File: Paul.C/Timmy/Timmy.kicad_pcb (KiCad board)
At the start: 2 copper layers, 34 parts, among them J1 I/O, J2 Power, J3 LED, SW1 SW_DIP_x02, U1 NJM4559

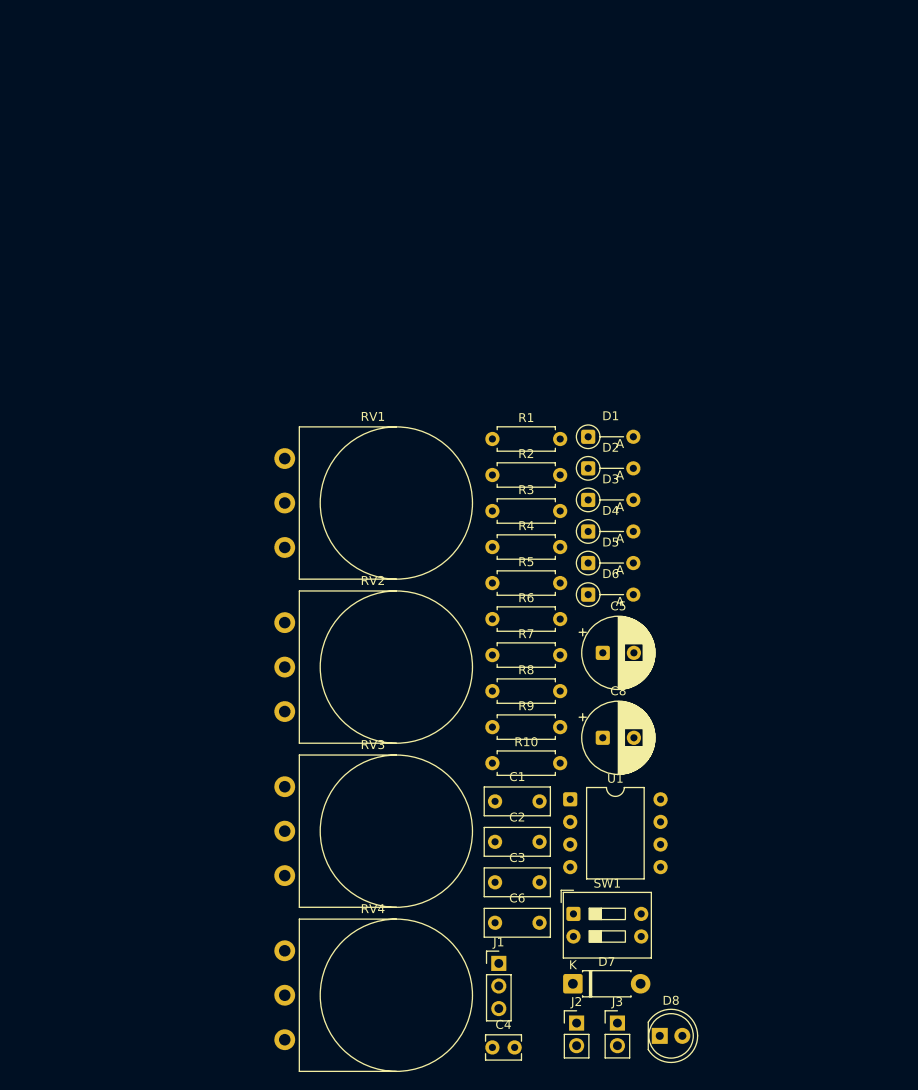
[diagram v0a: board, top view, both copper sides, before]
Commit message: feat: フットプリントを紐づけ
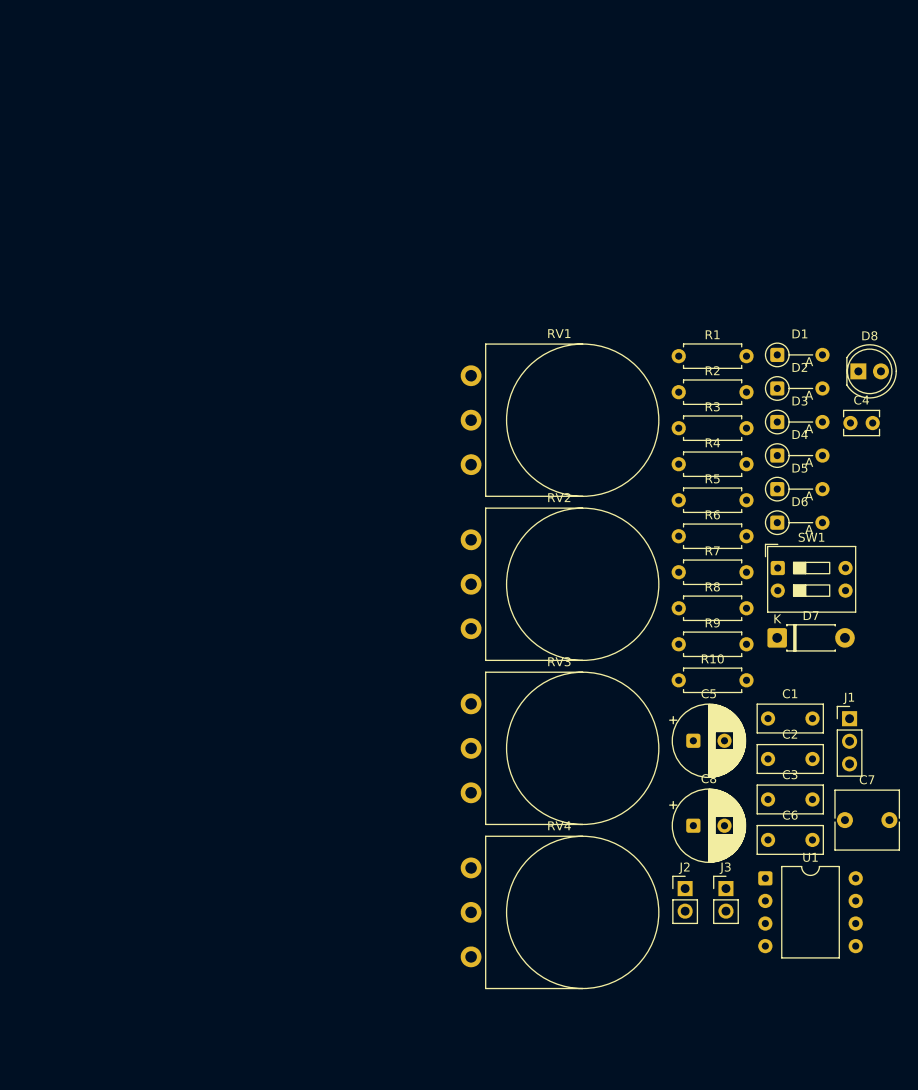
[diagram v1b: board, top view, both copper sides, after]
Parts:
- added C7: 1u, Capacitor_THT:C_Rect_L7.0mm_W6.5mm_P5.00mm, F.Cu at (170.5, 116.8)
- moved C4 80.9 mm to (171.1, 72.1)
- moved D8 78.0 mm to (172.0, 66.3)
- moved J1 48.1 mm to (171.0, 105.4)
- moved D7 45.2 mm to (162.9, 96.3)
- moved SW1 45.2 mm to (162.9, 88.4)
- moved C1 32.1 mm to (161.8, 105.3)
- moved C2 32.1 mm to (161.8, 109.9)
- moved C3 32.1 mm to (161.8, 114.5)
- moved C6 32.1 mm to (161.8, 119.0)
- moved U1 23.7 mm to (161.5, 123.3)
- moved D1 23.2 mm to (162.9, 64.5)
- moved D2 23.1 mm to (162.9, 68.2)
- moved D3 23.0 mm to (162.9, 72.0)
- moved RV1 22.9 mm to (128.4, 76.8)
- moved RV2 22.9 mm to (128.4, 95.2)
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
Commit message: feat: ReLayout Paul.C/Timmy
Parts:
- removed J1: I/O, Connector_PinHeader_2.54mm:PinHeader_1x03_P2.54mm_Vertical
- added J2: Power, Connector_PinHeader_2.54mm:PinHeader_1x02_P2.54mm_Vertical, F.Cu at (128.3, 55.8)
- added J5: INPUT, Connector_PinHeader_2.54mm:PinHeader_1x01_P2.54mm_Vertical, F.Cu at (97.8, 77.3)
- C4: value 100p -> 101
- D8, RV1, RV2, RV3: moved to B.Cu
- RV4: value A50k -> A10k; moved to B.Cu
- moved J3 93.3 mm to (99.8, 47.5), turned to 180 degrees
- moved J4 89.6 mm to (111.2, 47.5), turned to 180 degrees
- moved U1 83.4 mm to (100.4, 66.6)
- moved RV4 82.3 mm to (117.0, 50.7), turned to 90 degrees
- moved D5 80.8 mm to (82.6, 69.7), turned to 90 degrees
- moved D6 79.9 mm to (85.2, 64.7), turned to -90 degrees
- moved C2 78.3 mm to (92.9, 72.9)
- moved SW1 77.8 mm to (90.2, 60.8), turned to 180 degrees
- moved C6 75.3 mm to (97.9, 57.0), turned to 180 degrees
- moved D2 75.2 mm to (87.7, 69.7), turned to 90 degrees
- moved D7 74.5 mm to (101.7, 53.9)
- moved C7 74.2 mm to (123.3, 59.5), turned to 90 degrees
- moved C4 73.3 mm to (97.9, 69.1), turned to 90 degrees
- moved D1 72.6 mm to (90.2, 64.7), turned to -90 degrees
- moved C8 72.6 mm to (113.1, 57.0)
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- renumbered C6 to C5, C5 to C6, J2 to J3, J3 to J4
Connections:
- RV1 pad 3: unconnected-(RV1-Pad3) -> Net-(C1-Pad1)
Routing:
- net Net-(D5-K): track 0.00 -> 51.5 mm
- net Net-(D1-A): track 0.00 -> 49.6 mm
- net NEUT: track 0.00 -> 32.8 mm
- net +9V: track 0.00 -> 31.7 mm
- net Net-(U1B--): track 0.00 -> 17.5 mm
- net Net-(C7-Pad1): track 0.00 -> 16.4 mm
- net Net-(C3-Pad1): track 0.00 -> 15.8 mm
- net Net-(U1B-+): track 0.00 -> 14.7 mm
- net Net-(U1A-+): track 0.00 -> 12.5 mm
- net Net-(C1-Pad1): track 0.00 -> 10.9 mm
- net /INPUT: track 0.00 -> 9.35 mm
- net Net-(D8-A): track 0.00 -> 8.49 mm
- net Net-(R6-Pad1): track 0.00 -> 8.46 mm
- net Net-(D4-K): track 0.00 -> 8.41 mm
- net /OUTPUT: track 0.00 -> 8.38 mm
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- added copper zone on B.Cu, net GND
- added copper zone on F.Cu, net GND
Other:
- board outline added: 50.8 x 35.7 mm
- board text added: "+9V GND"
- board text added: "GND"
- board text added: "IN"
- board text added: "LED GND"
- board text added: "OUT"
- board text added: "Paul.C - Timmy [ReLayouted] 2026-08-22"

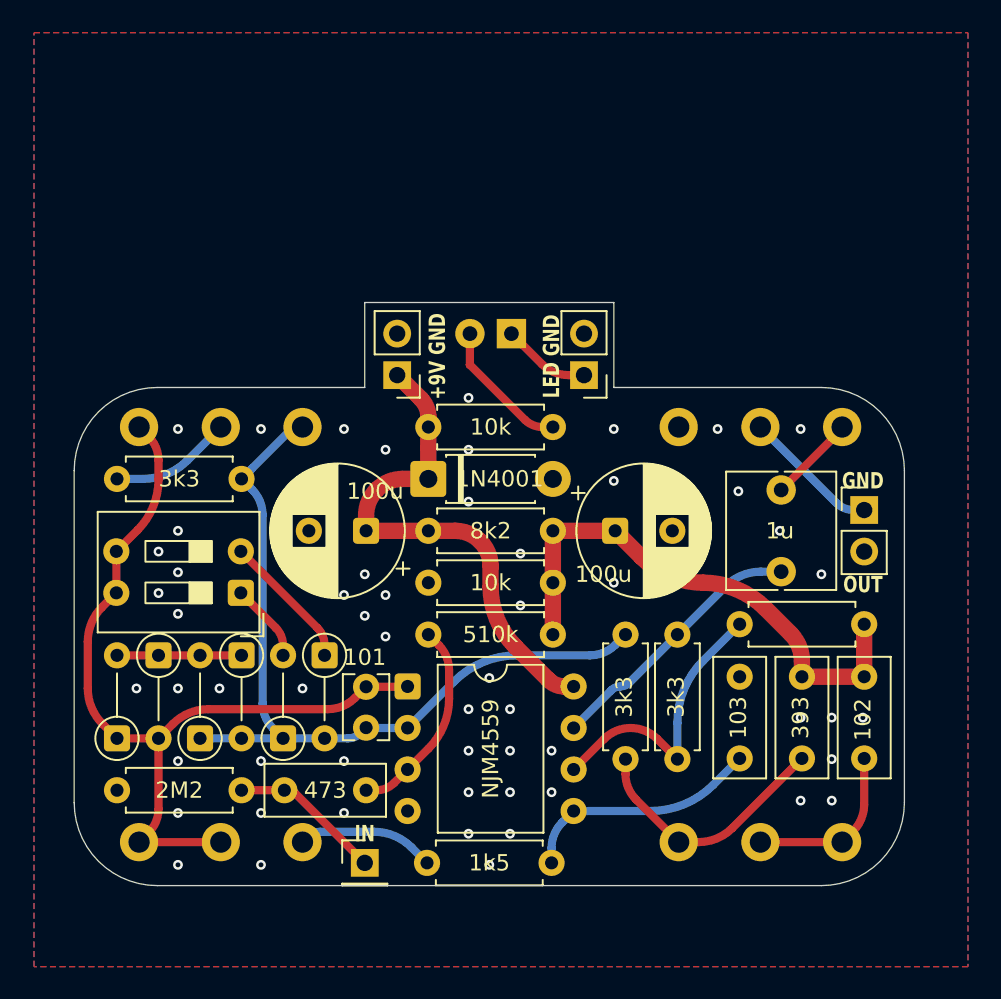
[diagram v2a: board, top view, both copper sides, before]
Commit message: fix: オペアンプのフットプリントを修正
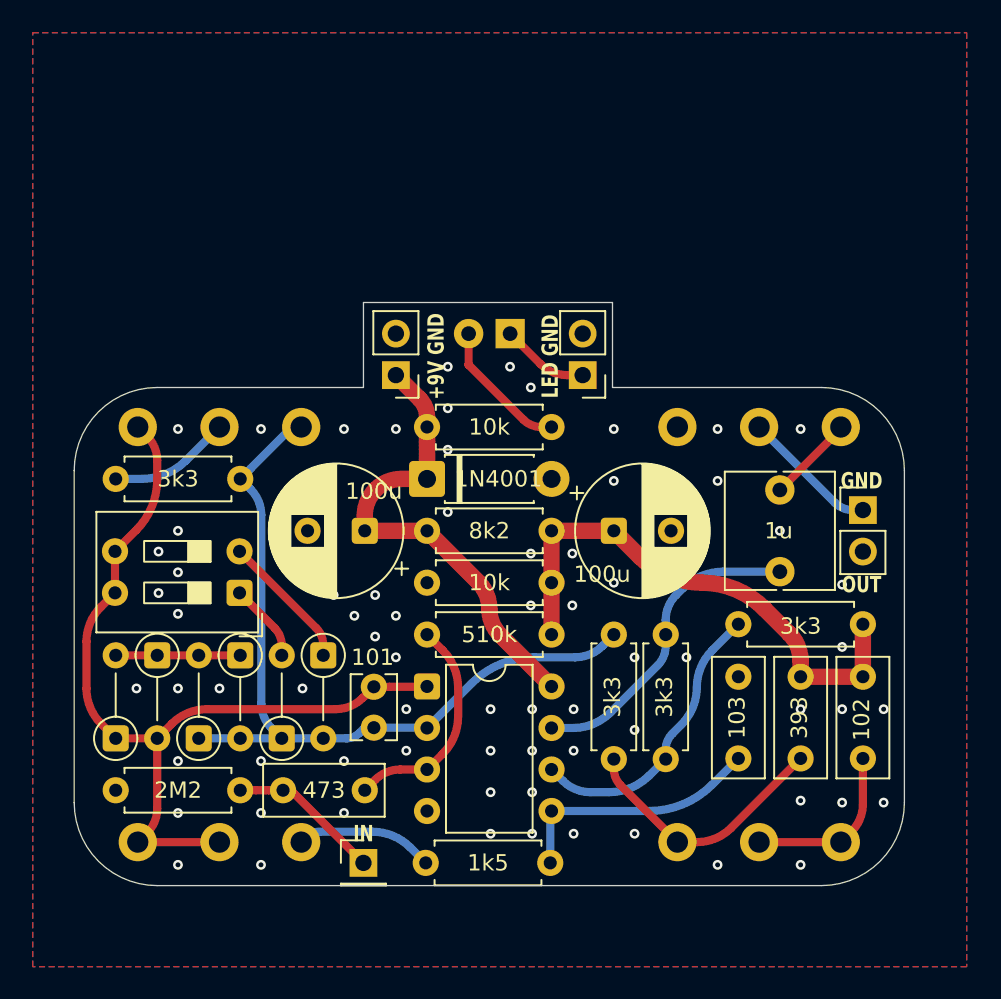
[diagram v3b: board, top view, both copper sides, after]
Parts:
- U1: footprint Package_DIP:DIP-8_W10.16mm -> Package_DIP:DIP-8_W7.62mm
- moved U1 1.19 mm to (101.6, 66.6)
- moved R3 0.72 mm to (113.0, 71.0)
- moved R7 0.72 mm to (116.2, 71.0)
- moved C4 0.47 mm to (98.3, 69.1)
- moved C3 0.08 mm to (124.5, 71.0)
- moved D3 0.08 mm to (92.7, 69.7)
- moved D7 0.08 mm to (101.6, 53.9)
- moved J3 0.08 mm to (99.7, 47.5)
- moved J5 0.08 mm to (97.7, 77.3)
- moved R10 0.08 mm to (101.6, 60.2)
- moved R2 0.08 mm to (101.6, 63.4)
- moved R8 0.08 mm to (101.6, 50.7)
- moved R9 0.08 mm to (101.6, 57.0)
- moved C2 0.08 mm to (92.8, 72.9)
- moved C5 0.08 mm to (120.7, 71.0)
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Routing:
- net +9V: track 31.7 -> 29.2 mm
- net Net-(C7-Pad1): track 16.4 -> 18.6 mm
- net Net-(U1A-+): track 12.5 -> 13.8 mm
- net Net-(D1-A): track 49.6 -> 48.4 mm
- net Net-(D5-K): track 51.5 -> 52.8 mm
- net Net-(U1B-+): track 14.7 -> 15.7 mm
- net GND: vias 60 -> 73
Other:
- outline, holes or cut-outs redrawn

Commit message: refactor: 見直しに伴う形式的な更新
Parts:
- renumbered J5 to J1
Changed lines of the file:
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@@
 		(descr "Through hole straight pin header, 1x01, 2.54mm pitch, single row")
 		(tags "Through hole pin header THT 1x01 2.54mm single row")
-		(property "Reference" "J5"
+		(property "Reference" "J1"
 			(at 0 -2.38 0)
 			(layer "F.SilkS")
